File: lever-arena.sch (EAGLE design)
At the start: 26 parts, among them J1 POWER_JACKPTH_BREAD

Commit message: Revision 2.3
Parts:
- REGULATOR: device spencer:POLULU5VREGULATOR -> spencer:POLULU5VREGULATORINVERTED
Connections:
- new net N$1: BNC0.1, PCB1.GPIO2
- new net N$5: BNC1.1, PCB1.GPIO3
- net N$3: no longer BNC0.1
- net N$6: no longer BNC1.1
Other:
- moved on the sheet: BNC0, BNC1
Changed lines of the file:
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@@
 <grid distance="0.1" unitdist="inch" unit="inch" style="lines" multiple="1" display="no" altdistance="0.01" altunitdist="inch" altunit="inch"/>
 <layers>
-<layer number="1" name="Top" color="4" fill="1" visible="no" active="no"/>
-<layer number="2" name="Route2" color="1" fill="3" visible="no" active="no"/>
-<layer number="3" name="Route3" color="4" fill="3" visible="no" active="no"/>
-<layer number="14" name="Route14" color="1" fill="6" visible="no" active="no"/>
-<layer number="15" name="Route15" color="4" fill="6" visible="no" active="no"/>
-<layer number="16" name="Bottom" color="1" fill="1" visible="no" active="no"/>
-<layer number="17" name="Pads" color="2" fill="1" visible="no" active="no"/>
-<layer number="18" name="Vias" color="2" fill="1" visible="no" active="no"/>
-<layer number="19" name="Unrouted" color="6" fill="1" visible="no" active="no"/>
-<layer number="20" name="Dimension" color="15" fill="1" visible="no" active="no"/>
-<layer number="21" name="tPlace" color="14" fill="1" visible="no" active="no"/>
-<layer number="22" name="bPlace" color="7" fill="1" visible="no" active="no"/>
-<layer number="23" name="tOrigins" color="15" fill="1" visible="no" active="no"/>
-<layer number="24" name="bOrigins" color="15" fill="1" visible="no" active="no"/>
-<layer number="25" name="tNames" color="7" fill="1" visible="no" active="no"/>
-<layer number="26" name="bNames" color="7" fill="1" visible="no" active="no"/>
-<layer number="27" name="tValues" color="7" fill="1" visible="no" active="no"/>
-<layer number="28" name="bValues" color="7" fill="1" visible="no" active="no"/>
+<layer number="1" name="Top" color="4" fill="1" visible="yes" active="no"/>
+<layer number="2" name="Route2" color="1" fill="3" visible="yes" active="no"/>
+<layer number="3" name="Route3" color="4" fill="3" visible="yes" active="no"/>
+<layer number="14" name="Route14" color="1" fill="6" visible="yes" active="no"/>
+<layer number="15" name="Route15" color="4" fill="6" visible="yes" active="no"/>
+<layer number="16" name="Bottom" color="1" fill="1" visible="yes" active="no"/>
+<layer number="17" name="Pads" color="2" fill="1" visible="yes" active="no"/>
+<layer number="18" name="Vias" color="2" fill="1" visible="yes" active="no"/>
+<layer number="19" name="Unrouted" color="6" fill="1" visible="yes" active="no"/>
+<layer number="20" name="Dimension" color="15" fill="1" visible="yes" active="no"/>
+<layer number="21" name="tPlace" color="7" fill="1" visible="yes" active="no"/>
+<layer number="22" name="bPlace" color="7" fill="1" visible="yes" active="no"/>
+<layer number="23" name="tOrigins" color="15" fill="1" visible="yes" active="no"/>
+<layer number="24" name="bOrigins" color="15" fill="1" visible="yes" active="no"/>
+<layer number="25" name="tNames" color="7" fill="1" visible="yes" active="no"/>
+<layer number="26" name="bNames" color="7" fill="1" visible="yes" active="no"/>
+<layer number="27" name="tValues" color="7" fill="1" visible="yes" active="no"/>
+<layer number="28" name="bValues" color="7" fill="1" visible="yes" active="no"/>
 <layer number="29" name="tStop" color="7" fill="3" visible="no" active="no"/>
 <layer number="30" name="bStop" color="7" fill="6" visible="no" active="no"/>
@@
 <layer number="35" name="tGlue" color="7" fill="4" visible="no" active="no"/>
 <layer number="36" name="bGlue" color="7" fill="5" visible="no" active="no"/>
-<layer number="37" name="tTest" color="7" fill="1" visible="no" active="no"/>
-<layer number="38" name="bTest" color="7" fill="1" visible="no" active="no"/>
+<layer number="37" name="tTest" color="7" fill="1" visible="yes" active="no"/>
+<layer number="38" name="bTest" color="7" fill="1" visible="yes" active="no"/>
 <layer number="39" name="tKeepout" color="4" fill="11" visible="no" active="no"/>
 <layer number="40" name="bKeepout" color="1" fill="11" visible="no" active="no"/>
@@
 <layer number="44" name="Drills" color="7" fill="1" visible="no" active="no"/>
 <layer number="45" name="Holes" color="7" fill="1" visible="no" active="no"/>
-<layer number="46" name="Milling" color="3" fill="1" visible="no" active="no"/>
-<layer number="47" name="Measures" color="7" fill="1" visible="no" active="no"/>
-<layer number="48" name="Document" color="7" fill="1" visible="no" active="no"/>
-<layer number="49" name="Reference" color="7" fill="1" visible="no" active="no"/>
-<layer number="50" name="dxf" color="7" fill="1" visible="no" active="no"/>
-<layer number="51" name="tDocu" color="7" fill="1" visible="no" active="no"/>
-<layer number="52" name="bDocu" color="7" fill="1" visible="no" active="no"/>
-<layer number="53" name="tGND_GNDA" color="7" fill="9" visible="no" active="no"/>
-<layer number="54" name="bGND_GNDA" color="1" fill="9" visible="no" active="no"/>
-<layer number="56" name="wert" color="7" fill="1" visible="no" active="no"/>
-<layer number="57" name="tCAD" color="7" fill="1" visible="no" active="no"/>
-<layer number="59" name="tCarbon" color="7" fill="1" visible="no" active="no"/>
-<layer number="60" name="bCarbon" color="7" fill="1" visible="no" active="no"/>
+<layer number="46" name="Milling" color="3" fill="1" visible="yes" active="no"/>
+<layer number="47" name="Measures" color="7" fill="1" visible="yes" active="no"/>
+<layer number="48" name="Document" color="7" fill="1" visible="yes" active="no"/>
+<layer number="49" name="Reference" color="7" fill="1" visible="yes" active="no"/>
+<layer number="50" name="dxf" color="7" fill="1" visible="yes" active="no"/>
+<layer number="51" name="tDocu" color="7" fill="1" visible="yes" active="no"/>
+<layer number="52" name="bDocu" color="7" fill="1" visible="yes" active="no"/>
+<layer number="53" name="tGND_GNDA" color="7" fill="9" visible="yes" active="no"/>
+<layer number="54" name="bGND_GNDA" color="1" fill="9" visible="yes" active="no"/>
+<layer number="56" name="wert" color="7" fill="1" visible="yes" active="no"/>
+<layer number="57" name="tCAD" color="7" fill="1" visible="yes" active="no"/>
+<layer number="59" name="tCarbon" color="7" fill="1" visible="yes" active="no"/>
+<layer number="60" name="bCarbon" color="7" fill="1" visible="yes" active="no"/>
 <layer number="90" name="Modules" color="5" fill="1" visible="yes" active="yes"/>
 <layer number="91" name="Nets" color="2" fill="1" visible="yes" active="yes"/>
@@
 <parts>
 <part name="PCB1" library="spencer" deviceset="RPI3" device=""/>
-<part name="REGULATOR" library="spencer" deviceset="POLULU5VREGULATOR" device="" value="REGULATOR"/>
+<part name="REGULATOR" library="spencer" deviceset="POLULU5VREGULATOR" device="INVERTED" value="REGULATOR"/>
 <part name="ADC0" library="spencer" deviceset="MCP3208" device=""/>
 <part name="ADC1" library="spencer" deviceset="MCP3208" device=""/>
@@
 <instance part="AIN" gate="A" x="-71.12" y="-86.36" rot="MR0"/>
 <instance part="3V3" gate="A" x="-111.76" y="-86.36"/>
-<instance part="BNC0" gate="G$1" x="-83.82" y="-71.12"/>
-<instance part="BNC1" gate="G$1" x="-71.12" y="-106.68"/>
+<instance part="BNC0" gate="G$1" x="-83.82" y="-17.78"/>
+<instance part="BNC1" gate="G$1" x="-83.82" y="-30.48"/>
 </instances>
 <busses>
@@
 <segment>
 <pinref part="BNC0" gate="G$1" pin="2"/>
-<junction x="-81.28" y="-73.66"/>
-<label x="-78.74" y="-73.66" size="1.27" layer="95" xref="yes"/>
+<junction x="-81.28" y="-20.32"/>
+<label x="-78.74" y="-20.32" size="1.27" layer="95" xref="yes"/>
 </segment>
 <segment>
 <pinref part="BNC1" gate="G$1" pin="2"/>
-<junction x="-68.58" y="-109.22"/>
-<label x="-66.04" y="-109.22" size="1.27" layer="95" xref="yes"/>
+<junction x="-81.28" y="-33.02"/>
+<label x="-78.74" y="-33.02" size="1.27" layer="95" xref="yes"/>
 </segment>
 </net>
@@
 <net name="N$3" class="0">
 <segment>
-<pinref part="BNC0" gate="G$1" pin="1"/>
-<junction x="-81.28" y="-71.12"/>
 <pinref part="AIN" gate="A" pin="1"/>
 <junction x="-68.58" y="-76.2"/>
@@
 <junction x="-60.96" y="-68.58"/>
 <wire x1="-68.58" y1="-76.2" x2="-60.96" y2="-76.2" width="0.1524" layer="91"/>
-<wire x1="-60.96" y1="-76.2" x2="-60.96" y2="-71.12" width="0.1524" layer="91"/>
-<wire x1="-60.96" y1="-71.12" x2="-60.96" y2="-68.58" width="0.1524" layer="91"/>
-<wire x1="-81.28" y1="-71.12" x2="-60.96" y2="-71.12" width="0.1524" layer="91"/>
-<junction x="-60.96" y="-71.12"/>
+<wire x1="-60.96" y1="-76.2" x2="-60.96" y2="-68.58" width="0.1524" layer="91"/>
 </segment>
 </net>
 <net name="N$6" class="0">
 <segment>
-<pinref part="BNC1" gate="G$1" pin="1"/>
-<junction x="-68.58" y="-106.68"/>
 <pinref part="AIN" gate="A" pin="8"/>
 <junction x="-68.58" y="-93.98"/>
@@
 <wire x1="-68.58" y1="-93.98" x2="-43.18" y2="-93.98" width="0.1524" layer="91"/>
 <wire x1="-43.18" y1="-93.98" x2="-43.18" y2="-68.58" width="0.1524" layer="91"/>
-<wire x1="-68.58" y1="-106.68" x2="-43.18" y2="-106.68" width="0.1524" layer="91"/>
-<wire x1="-43.18" y1="-106.68" x2="-43.18" y2="-93.98" width="0.1524" layer="91"/>
-<junction x="-43.18" y="-93.98"/>
-</segment>
-</net>
+</segment>
+</net>
+<net name="N$1" class="0">
+<segment>
+<pinref part="BNC0" gate="G$1" pin="1"/>
+<junction x="-81.28" y="-17.78"/>
+<pinref part="PCB1" gate="G$1" pin="GPIO2"/>
+<junction x="-43.18" y="-12.7"/>
+<wire x1="-81.28" y1="-17.78" x2="-43.18" y2="-17.78" width="0.1524" layer="91"/>
+<wire x1="-43.18" y1="-17.78" x2="-43.18" y2="-12.7" width="0.1524" layer="91"/>
+</segment>
+</net>
+<net name="N$5" class="0">
+<segment>
+<pinref part="BNC1" gate="G$1" pin="1"/>
+<junction x="-81.28" y="-30.48"/>
+<pinref part="PCB1" gate="G$1" pin="GPIO3"/>
+<junction x="-38.1" y="-12.7"/>
+<wire x1="-81.28" y1="-30.48" x2="-38.1" y2="-30.48" width="0.1524" layer="91"/>
+<wire x1="-38.1" y1="-30.48" x2="-38.1" y2="-12.7" width="0.1524" layer="91"/>
+</segment>
+</net>

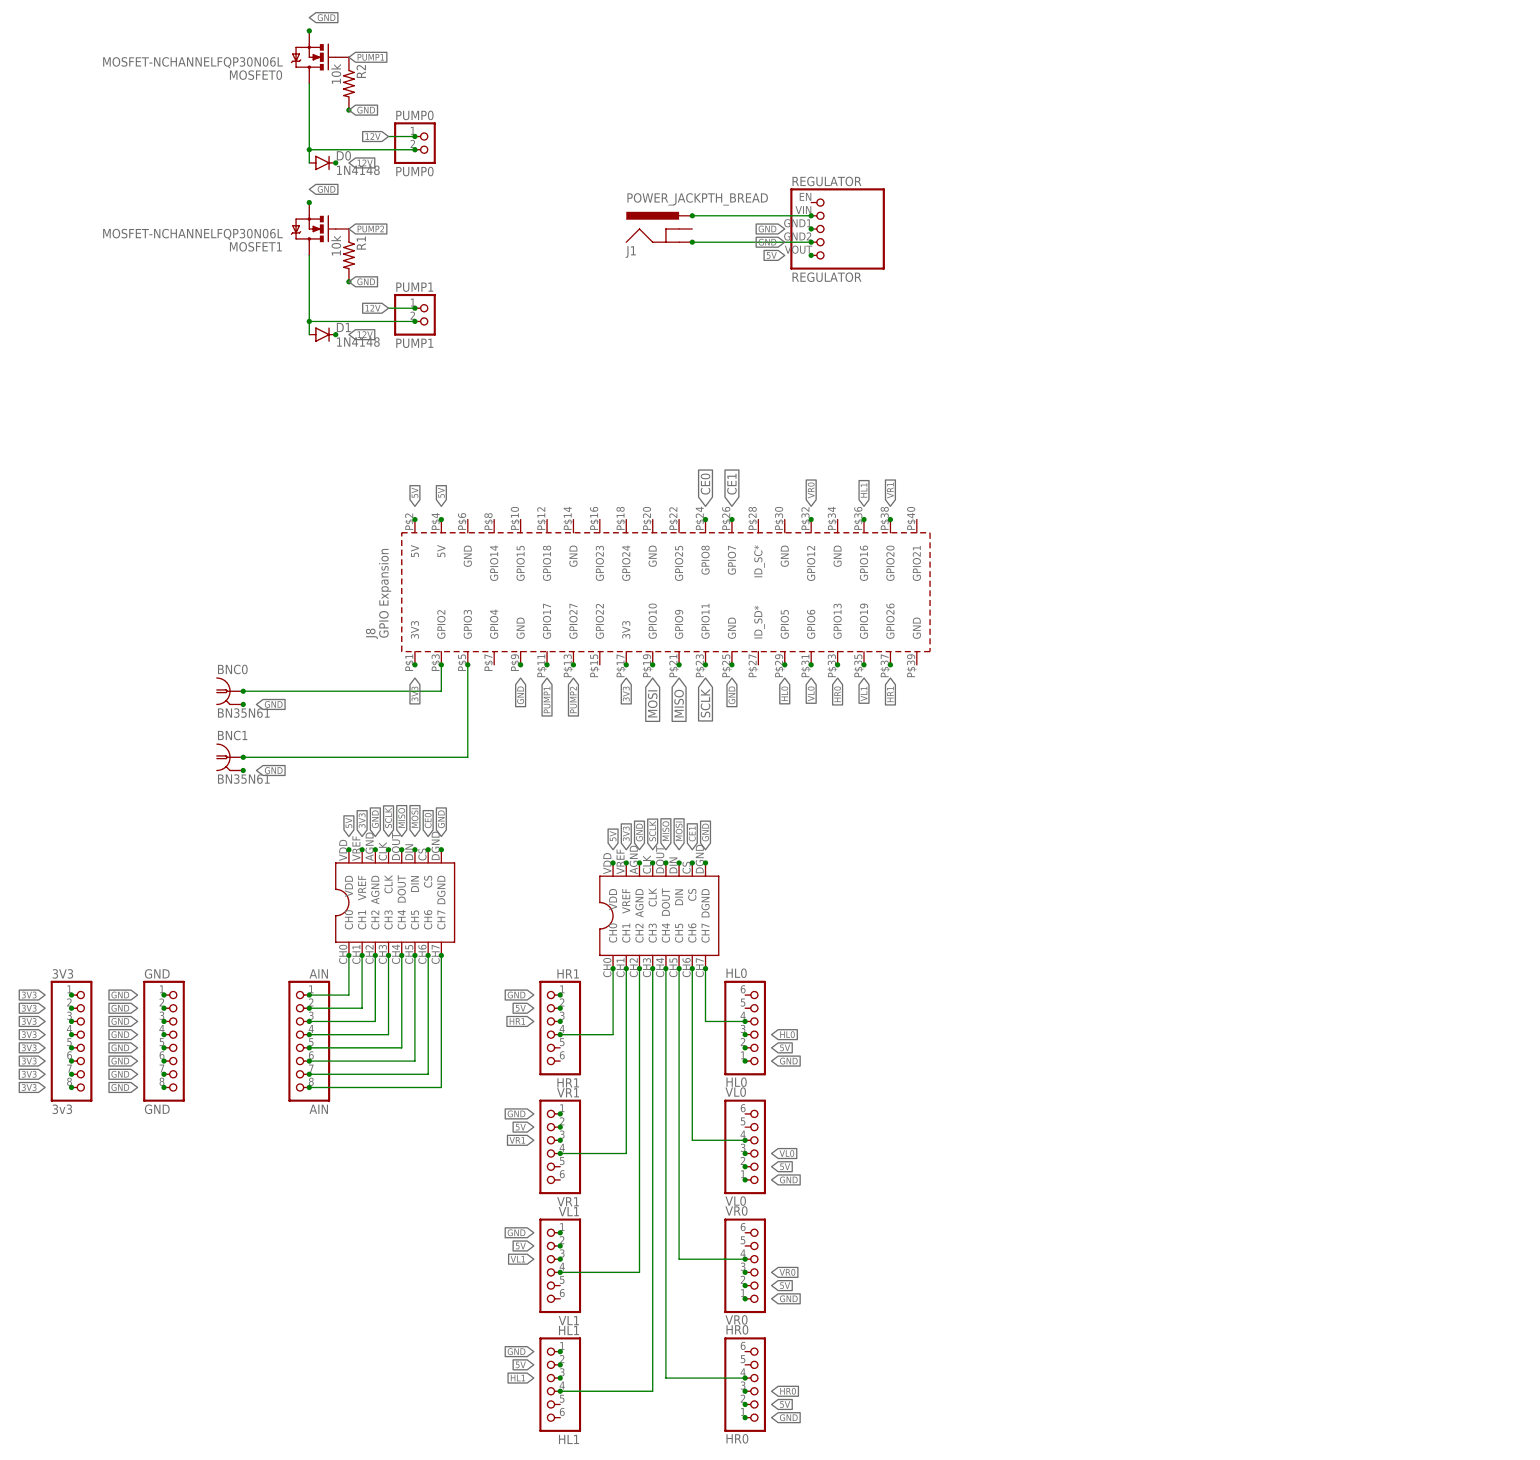
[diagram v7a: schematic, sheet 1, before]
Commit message: Revision 2.4
routed connectors for adc input
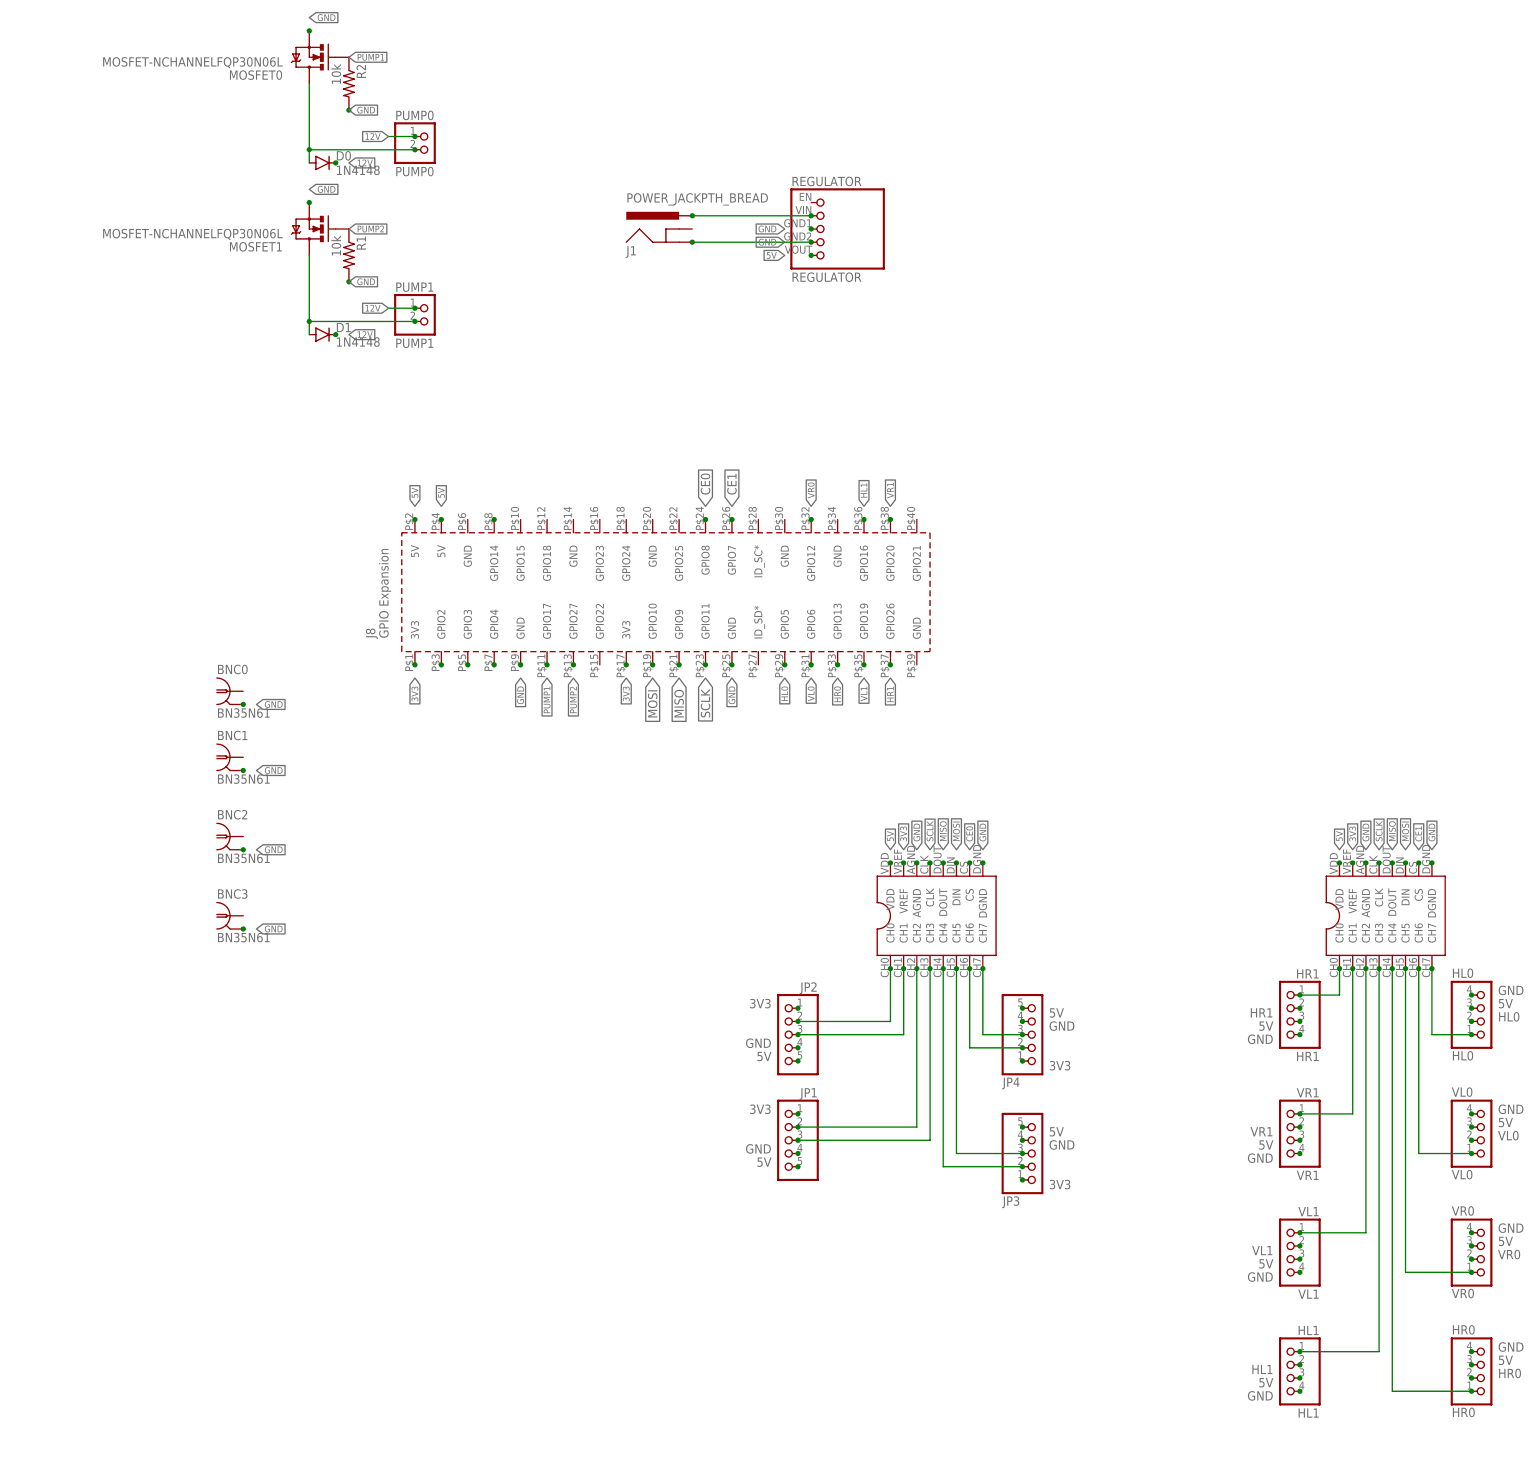
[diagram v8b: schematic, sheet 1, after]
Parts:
- removed 3V3: 3v3, pinhead:PINHD-1X8
- removed AIN: AIN, pinhead:PINHD-1X8
- removed GND: GND, pinhead:PINHD-1X8
- added BNC2, BNC3: BN35N61, con-coax:BN35N61
- added JP1, JP2, JP3, JP4: (no value), pinhead:PINHD-1X5
- HL0, HL1, HR0, HR1, VL0, VL1, VR0, VR1: device pinhead:PINHD-1X6 -> pinhead:PINHD-1X4
- REGULATOR: device spencer:POLULU5VREGULATORINVERTED -> spencer:POLULU5VREGULATORNORMAL
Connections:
- removed net N$11: ADC0.CH1, AIN.2
- removed net N$22: ADC1.CH7, HL0.4
- removed net N$23: ADC1.CH6, VL0.4
- removed net N$27: ADC1.CH5, VR0.4
- removed net N$29: ADC1.CH0, HR1.4
- removed net N$31: ADC1.CH1, VR1.4
- removed net N$6: ADC0.CH7, AIN.8
- new net N$17: ADC0.CH0, JP2.2
- new net N$20: ADC1.CH5, VR0.1
- new net N$34: ADC0.CH4, JP3.2
- new net N$36: ADC1.CH1, VR1.1
- new net N$39: ADC0.CH7, JP4.3
- new net N$40: ADC0.CH6, JP4.2
- new net N$7: PCB1.GPIO3
- new net N$8: PCB1.GPIO2
- new net NGNG: ADC1.CH4, HR0.1
- net 3V3: now also JP1.1, JP2.1, JP3.1, JP4.1; no longer 3V3.1, 3V3.2, 3V3.3, 3V3.4, 3V3.5, 3V3.6, 3V3.7, 3V3.8
- net 5V: now also HL0.3, HL1.3, HR0.3, HR1.3, JP1.5, JP2.5, JP3.5, JP4.5, VL0.3, VL1.3, VR0.3, VR1.3; no longer HL0.2, HL1.2, HR0.2, HR1.2, VL0.2, VL1.2, VR0.2, VR1.2
- net GND: now also BNC2.2, BNC3.2, HL0.4, HL1.4, HR0.4, HR1.4, JP1.4, JP2.4, JP3.4, JP4.4, VL0.4, VL1.4, VR0.4, VR1.4; no longer GND.1, GND.2, GND.3, GND.4, GND.5, GND.6, GND.7, GND.8, HL0.1, HL1.1, HR0.1, HR1.1, VL0.1, VL1.1, VR0.1, VR1.1
- net HL0: now also HL0.2; no longer HL0.3
- net HL1: now also HL1.2; no longer HL1.3
- net HR0: now also HR0.2; no longer HR0.3
- net HR1: now also HR1.2; no longer HR1.3
- net N$1: now also PCB1.GPIO14; no longer BNC0.1, PCB1.GPIO2
- net N$12: now also ADC1.CH7, HL0.1; no longer ADC0.CH2, AIN.3
- net N$13: now also JP1.3; no longer AIN.4
- net N$14: now also ADC0.CH2, JP1.2; no longer ADC0.CH4, AIN.5
- net N$15: now also ADC0.CH1, JP2.3; no longer ADC0.CH5, AIN.6
- net N$16: now also ADC1.CH6, VL0.1; no longer ADC0.CH6, AIN.7
- net N$28: now also ADC1.CH3, HL1.1; no longer ADC1.CH4, HR0.4
- net N$3: now also ADC1.CH0, HR1.1; no longer ADC0.CH0, AIN.1
- net N$32: now also VL1.1; no longer VL1.4
- net N$33: now also ADC0.CH5, JP3.3; no longer ADC1.CH3, HL1.4
- net N$5: now also PCB1.GPIO4; no longer BNC1.1, PCB1.GPIO3
- net VL0: now also VL0.2; no longer VL0.3
- net VL1: now also VL1.2; no longer VL1.3
- net VR0: now also VR0.2; no longer VR0.3
- net VR1: now also VR1.2; no longer VR1.3
